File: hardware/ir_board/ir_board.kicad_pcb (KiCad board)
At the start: 2 copper layers, 25.2 x 30 mm, 22 parts, among them J1 Conn_01x04, J2 Conn_01x06, Q1 IRLML0030, U1 VL53L0CXV0DH1

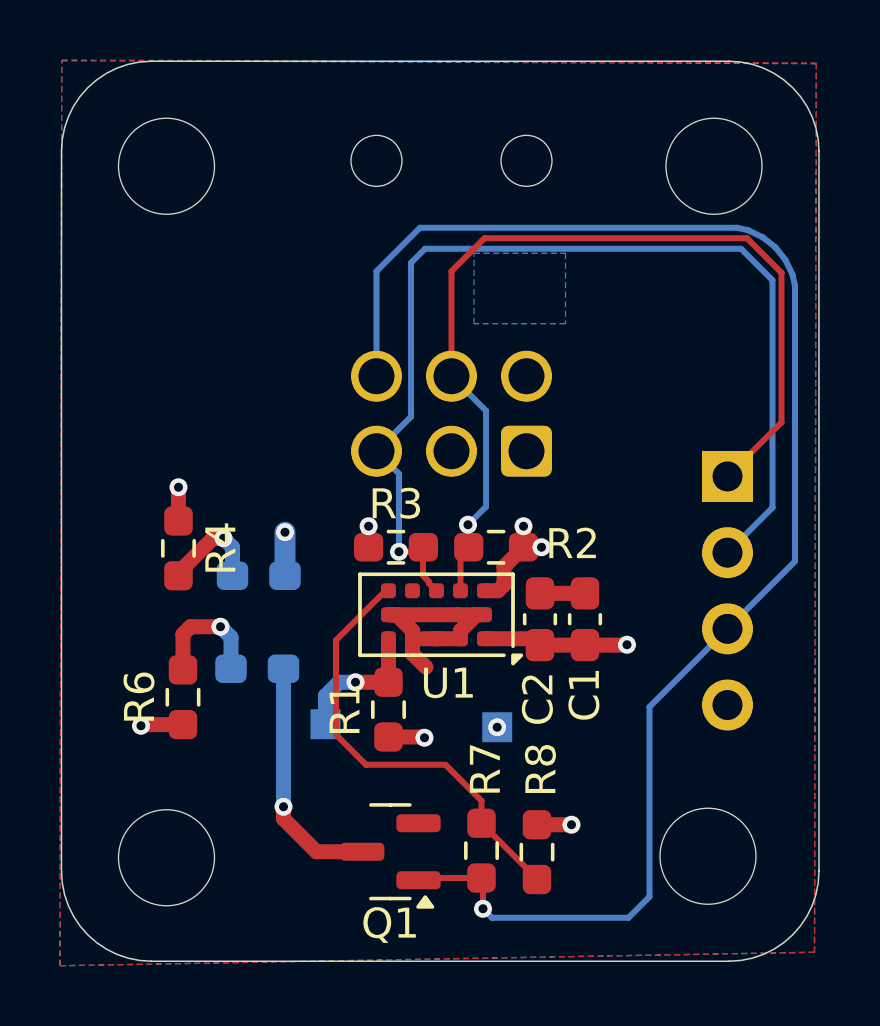
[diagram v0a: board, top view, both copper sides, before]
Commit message: Pitot Board Rev B (#3)
* init

* added layout

* ready to review

* finished pitot board

* pitot board ordered, routing+size finished for temperature board so pull??

* finished tempboard silkscreen

* resized temperature board

* poo oo ee

* ughhhhhhhhhhhhhhhhhhghghghhhhhhhhhhhhhhhhhhh

* working i2c on RH board

* cleanup?

* small

* added read me

* fixed mistake

* Fix image filename case in README.md

* Add new line for telemetry components explanation
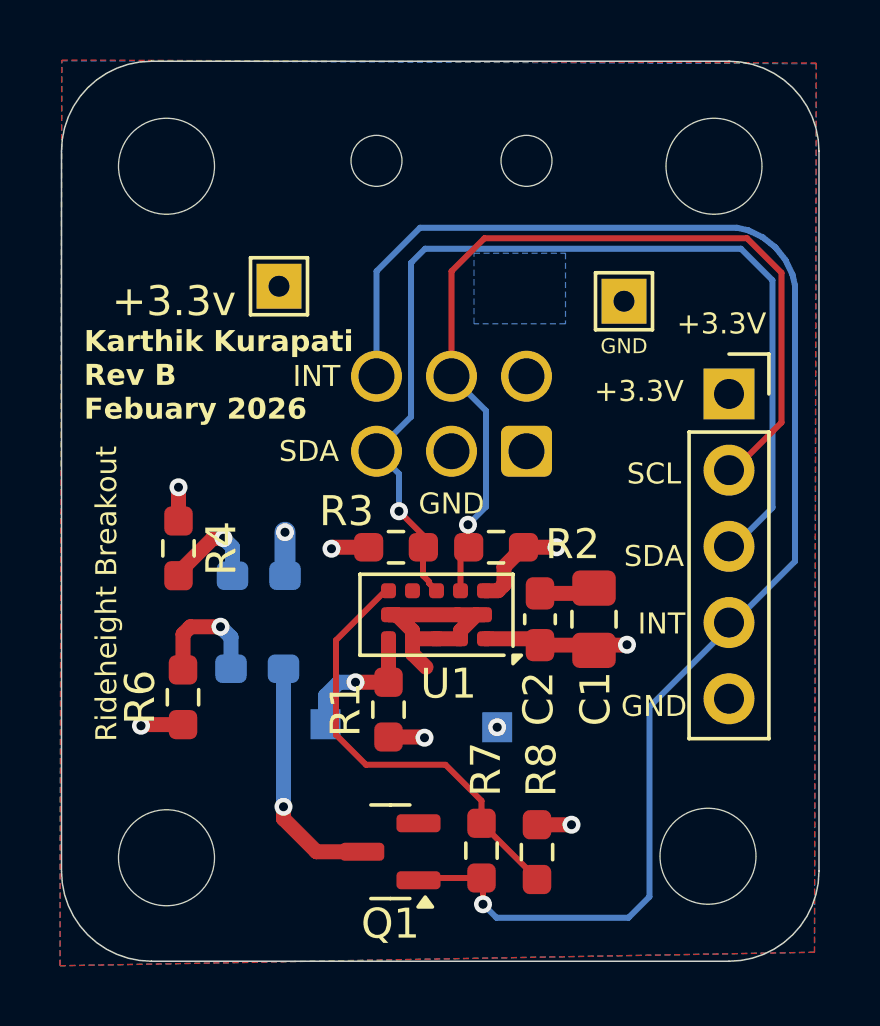
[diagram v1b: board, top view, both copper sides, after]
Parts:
- removed G***: LHRs_LOGO, UTSVT_Logos:LHRs_LOGO
- added +3.3v: TestPoint, TestPoint:TestPoint_THTPad_1.5x1.5mm_Drill0.7mm, F.Cu at (155.5, 56.8)
- added GND: TestPoint, TestPoint:TestPoint_THTPad_1.5x1.5mm_Drill0.7mm, F.Cu at (167.0, 57.2)
- C1: value 10uf -> 4.7uf; footprint Capacitor_SMD:C_0603_1608Metric_Pad1.08x0.95mm_HandSolder -> Capacitor_SMD:C_0805_2012Metric_Pad1.18x1.45mm_HandSolder
- J1: value Conn_01x04 -> Conn_01x05; footprint Connector_PinHeader_2.54mm:PinHeader_1x04_P2.54mm_Vertical -> Connector_PinSocket_2.54mm:PinSocket_1x05_P2.54mm_Vertical; moved to F.Cu
- moved J1 2.75 mm to (170.5, 60.3), turned to 0 degrees
- moved C1 0.30 mm to (166.0, 67.8)
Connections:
- J1 pad 1: /SCL -> +3.3V
- J1 pad 2: /SDA -> /SCL
- J1 pad 3: /GPIO1 -> /SDA
- J1 pad 4: GND -> /GPIO1
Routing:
- net /SDA: track 35.3 -> 34.6 mm
- net +3.3V: track 14.0 -> 14.4 mm, vias 8 -> 7
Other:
- board text added: "+3.3V"
- board text added: "GND"
- board text added: "INT"
- board text added: "Karthik Kurapati Rev B Febuary 2026"
- board text added: "Rideheight Breakout"
- board text added: "SCL"
- board text added: "SDA"
- board text removed: "3.3V"
